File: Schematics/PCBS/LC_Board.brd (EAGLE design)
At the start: 160 x 100 mm, 24 parts, among them IC1 ATMEGA328P-AU, Q10 220mA/50V/3.5Ω, U1 LT1763CS8-3.3#TRPBF

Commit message: routing for PCB 1  ok outcome
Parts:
- RESET_PULLUP: device audio amplifier example:R0402 -> audio amplifier example:R0603
- moved RESET_PULLUP 26.9 mm to (44.5, 12.7)
- moved JP3 16.5 mm to (12.7, 39.4), turned to 0 degrees
- moved LED3BLUE 14.2 mm to (110.5, 12.7), turned to 180 degrees
- moved E1 13.5 mm to (43.2, 40.6), turned to 90 degrees
- moved LED1BLUE 13.3 mm to (110.5, 25.4), turned to 180 degrees
- moved LED3RED 13.3 mm to (110.5, 20.3)
- moved LED1RED 12.8 mm to (110.5, 33.0)
- moved LED2BLUE 12.8 mm to (110.5, 38.1), turned to 180 degrees
- moved LED2RED 12.8 mm to (110.5, 45.7)
- moved C1 11.4 mm to (19.2, 28.2), turned to 90 degrees
- moved LED3GREEN 10.2 mm to (106.7, 16.5), turned to 90 degrees
- moved E2 9.92 mm to (45.7, 40.6), turned to 90 degrees
- moved LED1GREEN 9.25 mm to (106.7, 29.2), turned to 90 degrees
- moved D3 8.98 mm to (110.5, 16.5)
- moved LED2GREEN 8.89 mm to (106.7, 41.9), turned to 90 degrees
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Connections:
- net N$1 renamed RED1
- net N$15 renamed RESET_LINE
- net N$2 renamed GREEN1
- net N$3 renamed BLUE1
- net N$4 renamed RED2
- net N$5 renamed GREEN2
- net N$6 renamed BLUE2
- net N$7 renamed RED3
- net N$8 renamed GREEN3
- net N$9 renamed BLUE3
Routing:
- net GND: track 0.00 -> 248.4 mm, vias 0 -> 1
- net 3.3V_RAIL: track 0.00 -> 204.9 mm
- net D5: track 0.00 -> 77.5 mm, vias 0 -> 2
- net D10: track 0.00 -> 75.2 mm, vias 0 -> 2
- net D8: track 0.00 -> 74.1 mm, vias 0 -> 2
- net D7: track 0.00 -> 72.6 mm, vias 0 -> 2
- net D9: track 0.00 -> 71.4 mm, vias 0 -> 2
- net D13: track 0.00 -> 68.8 mm
- net D6: track 0.00 -> 67.1 mm, vias 0 -> 2
- net D11: track 0.00 -> 65.9 mm, vias 0 -> 2
- net D12: track 0.00 -> 64.6 mm, vias 0 -> 2
- net RDI: track 0.00 -> 50.0 mm
- net TXO: track 0.00 -> 39.2 mm, vias 0 -> 1
- net RDI2: track 0.00 -> 34.9 mm
- net RESET_LINE: track 0.00 -> 34.2 mm
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
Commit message: LC_board PCB pos nearing finish for R1
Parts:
- moved JP2 73.8 mm to (86.4, 30.5), turned to 270 degrees
- moved C1 70.5 mm to (88.9, 17.8), turned to 180 degrees
- moved JP3 64.1 mm to (76.2, 30.5), turned to 90 degrees
- moved CONVERTEPULLUP 61.2 mm to (81.3, 26.7)
- moved Q10 61.0 mm to (81.3, 33.0)
- moved U1 54.6 mm to (83.8, 11.4)
- moved E1 50.9 mm to (94.0, 38.1)
- moved E2 50.9 mm to (96.5, 38.1)
- moved C2 50.8 mm to (96.4, 7.87)
- moved RESET_PULLUP 50.4 mm to (94.9, 11.7)
- moved IC1 49.5 mm to (94.0, 29.2)
- moved JP1 49.5 mm to (94.0, 2.54)
- moved LED1RED 14.0 mm to (110.5, 19.1)
- moved D1 14.0 mm to (110.5, 15.2), flipped to the bottom, turned to 180 degrees
- moved LED1GREEN 14.0 mm to (106.7, 15.2)
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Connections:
- net RXI2 renamed S$1
- net 3.3V_RAIL: no longer JP1.4
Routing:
- net GND: track 248.4 -> 136.4 mm, vias 1 -> 2
- net 3.3V_RAIL: track 204.9 -> 96.3 mm, vias 0 -> 3
- net D10: track 75.2 -> 0.00 mm, vias 2 -> 0
- net D13: track 68.8 -> 0.00 mm
- net D8: track 74.1 -> 7.75 mm, vias 2 -> 0
- net D11: track 65.9 -> 0.00 mm, vias 2 -> 0
- net D9: track 71.4 -> 6.27 mm, vias 2 -> 0
- net D12: track 64.6 -> 0.00 mm, vias 2 -> 0
- net D5: track 77.5 -> 26.7 mm
- net D6: track 67.1 -> 24.5 mm
- net D7: track 72.6 -> 30.7 mm
- net RDI: track 50.0 -> 33.6 mm
- net RDI2: track 34.9 -> 23.9 mm
- net RDI_3.3V: track 3.84 -> 12.3 mm
- net RESET_LINE: track 34.2 -> 36.3 mm, vias 0 -> 2
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
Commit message: back up be for remixing LED pos
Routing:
- net D8: track 7.75 -> 31.9 mm, vias 0 -> 1
- net D10: track 0.00 -> 23.0 mm, vias 0 -> 1
- net D11: track 0.00 -> 14.7 mm, vias 0 -> 1
- net D13: track 0.00 -> 13.5 mm, vias 0 -> 1
- net D9: track 6.27 -> 19.5 mm, vias 0 -> 1
- net D12: track 0.00 -> 12.6 mm, vias 0 -> 1
- net 3.3V_RAIL: track 96.3 -> 103.6 mm
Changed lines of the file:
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@@
 <wire x1="97.3853125" y1="27.4814" x2="96.8567125" y2="28.01" width="0.1524" layer="1"/>
 <contactref element="IC1" pad="6"/>
-<wire x1="96.8567125" y1="28.01" x2="93.98" y2="28.01" width="0.1524" layer="1"/>
-<wire x1="93.98" y1="28.01" x2="89.73" y2="28.01" width="0.1524" layer="1"/>
+<wire x1="96.8567125" y1="28.01" x2="95.25" y2="28.01" width="0.1524" layer="1"/>
+<wire x1="95.25" y1="28.01" x2="92.71" y2="28.01" width="0.1524" layer="1"/>
+<wire x1="92.71" y1="28.01" x2="89.73" y2="28.01" width="0.1524" layer="1"/>
 <wire x1="89.73" y1="28.01" x2="89.4586" y2="28.2814" width="0.1524" layer="1"/>
 <contactref element="C1" pad="+"/>
 <wire x1="90.17" y1="17.399" x2="89.789" y2="17.78" width="0.1524" layer="1"/>
 <contactref element="D3" pad="4"/>
-<wire x1="113.03" y1="27.94" x2="113.03" y2="21.59" width="0.1524" layer="16"/>
-<wire x1="113.03" y1="21.59" x2="113.03" y2="16.51" width="0.1524" layer="16"/>
-<wire x1="112.53" y1="28.44" x2="113.03" y2="27.94" width="0.1524" layer="16"/>
-<wire x1="112.53" y1="28.44" x2="111.19" y2="28.44" width="0.1524" layer="16"/>
-<wire x1="113.03" y1="27.94" x2="113.03" y2="40.64" width="0.1524" layer="16"/>
-<wire x1="113.03" y1="40.64" x2="112.53" y2="41.14" width="0.1524" layer="16"/>
-<wire x1="112.53" y1="41.14" x2="111.19" y2="41.14" width="0.1524" layer="16"/>
+<wire x1="114.3" y1="27.94" x2="114.3" y2="22.86" width="0.1524" layer="16"/>
+<wire x1="114.3" y1="20.32" x2="114.3" y2="16.51" width="0.1524" layer="16"/>
+<wire x1="113.8" y1="28.44" x2="114.3" y2="27.94" width="0.1524" layer="16"/>
+<wire x1="113.8" y1="28.44" x2="111.19" y2="28.44" width="0.1524" layer="16"/>
+<wire x1="114.3" y1="27.94" x2="114.3" y2="40.64" width="0.1524" layer="16"/>
+<wire x1="114.3" y1="40.64" x2="113.8" y2="41.14" width="0.1524" layer="16"/>
+<wire x1="113.8" y1="41.14" x2="111.19" y2="41.14" width="0.1524" layer="16"/>
 <contactref element="D1" pad="4"/>
 <wire x1="98.23" y1="27.21" x2="101.06" y2="27.21" width="0.1524" layer="1"/>
@@
 <via x="106.68" y="21.59" extent="1-16" drill="0.35" shape="octagon"/>
 <wire x1="106.68" y1="21.59" x2="113.03" y2="21.59" width="0.1524" layer="16"/>
-<wire x1="113.03" y1="16.51" x2="112.26" y2="15.74" width="0.1524" layer="16"/>
-<wire x1="112.26" y1="15.74" x2="111.19" y2="15.74" width="0.1524" layer="16"/>
+<wire x1="114.3" y1="16.51" x2="113.53" y2="15.74" width="0.1524" layer="16"/>
+<wire x1="113.53" y1="15.74" x2="111.19" y2="15.74" width="0.1524" layer="16"/>
 <wire x1="80.43" y1="26.67" x2="80.33" y2="26.77" width="0.1524" layer="1"/>
 <wire x1="80.33" y1="26.77" x2="80.33" y2="32.02" width="0.1524" layer="1"/>
@@
 <wire x1="93.98" y1="15.24" x2="93.98" y2="26.67" width="0.1524" layer="16"/>
 <via x="93.98" y="26.67" extent="1-16" drill="0.35" shape="octagon"/>
-<wire x1="93.98" y1="26.67" x2="93.98" y2="28.01" width="0.1524" layer="1"/>
 <contactref element="U1" pad="1"/>
 <wire x1="85.725" y1="13.8938" x2="89.6112" y2="17.78" width="0.1524" layer="1"/>
 <wire x1="89.6112" y1="17.78" x2="89.789" y2="17.78" width="0.1524" layer="1"/>
+<wire x1="113.03" y1="21.59" x2="114.3" y2="22.86" width="0.1524" layer="16"/>
+<wire x1="113.03" y1="21.59" x2="114.3" y2="20.32" width="0.1524" layer="16"/>
+<wire x1="92.71" y1="28.01" x2="93.98" y2="26.74" width="0.1524" layer="1"/>
+<wire x1="93.98" y1="26.74" x2="93.98" y2="26.67" width="0.1524" layer="1"/>
+<wire x1="95.25" y1="28.01" x2="95.25" y2="27.94" width="0.1524" layer="1"/>
+<wire x1="95.25" y1="27.94" x2="93.98" y2="26.67" width="0.1524" layer="1"/>
 <wire x1="97.79" y1="27.4814" x2="98.23" y2="27.21" width="0" layer="19" extent="1-1"/>
 <wire x1="80.43" y1="26.67" x2="89.73" y2="28.01" width="0" layer="19" extent="1-1"/>
@@
 <wire x1="99.06" y1="38.1" x2="96.52" y2="38.1" width="0.1524" layer="1"/>
 <wire x1="100.33" y1="29.61" x2="100.33" y2="36.83" width="0.1524" layer="1"/>
-<wire x1="110.49" y1="35.73" x2="110.49" y2="35.56" width="0" layer="19" extent="1-1"/>
+<wire x1="110.49" y1="45.55" x2="110.49" y2="35.56" width="0" layer="19" extent="1-1"/>
 <wire x1="97.79" y1="29.3386" x2="98.23" y2="29.61" width="0" layer="19" extent="1-1"/>
 <wire x1="83.185" y1="8.9662" x2="83.185" y2="8.255" width="0" layer="19" extent="1-1"/>
@@
 <contactref element="IC1" pad="13"/>
 <contactref element="LED2GREEN" pad="1"/>
-<wire x1="96.52" y1="20.32" x2="107.78" y2="39.69" width="0" layer="19" extent="1-1"/>
 <wire x1="94.38" y1="24.96" x2="94.38" y2="21.19" width="0.1524" layer="1"/>
 <wire x1="94.38" y1="21.19" x2="95.25" y2="20.32" width="0.1524" layer="1"/>
 <wire x1="95.25" y1="20.32" x2="96.52" y2="20.32" width="0.1524" layer="1"/>
+<wire x1="107.78" y1="39.69" x2="107.78" y2="39.2" width="0.1524" layer="1"/>
+<wire x1="107.78" y1="39.2" x2="106.68" y2="38.1" width="0.1524" layer="1"/>
+<via x="106.68" y="38.1" extent="1-16" drill="0.35" shape="octagon"/>
+<wire x1="106.68" y1="38.1" x2="105.41" y2="39.37" width="0.1524" layer="16"/>
+<wire x1="105.41" y1="39.37" x2="104.14" y2="39.37" width="0.1524" layer="16"/>
+<wire x1="104.14" y1="39.37" x2="102.87" y2="38.1" width="0.1524" layer="16"/>
+<wire x1="102.87" y1="38.1" x2="102.87" y2="31.75" width="0.1524" layer="16"/>
+<wire x1="94.38" y1="24.96" x2="102.87" y2="31.75" width="0" layer="19" extent="1-16"/>
 </signal>
 <signal name="D10">
 <contactref element="IC1" pad="14"/>
 <contactref element="LED2BLUE" pad="1"/>
-<wire x1="95.18" y1="24.96" x2="111.44" y2="37.93" width="0" layer="19" extent="1-1"/>
+<wire x1="95.18" y1="24.96" x2="95.18" y2="22.93" width="0.1524" layer="1"/>
+<wire x1="95.18" y1="22.93" x2="96.52" y2="21.59" width="0.1524" layer="1"/>
+<wire x1="96.52" y1="21.59" x2="100.33" y2="21.59" width="0.1524" layer="1"/>
+<wire x1="111.44" y1="37.93" x2="111.93" y2="37.93" width="0.1524" layer="1"/>
+<wire x1="111.93" y1="37.93" x2="113.03" y2="36.83" width="0.1524" layer="1"/>
+<via x="113.03" y="36.83" extent="1-16" drill="0.35" shape="octagon"/>
+<wire x1="113.03" y1="36.83" x2="105.41" y2="36.83" width="0.1524" layer="16"/>
+<wire x1="105.41" y1="36.83" x2="104.14" y2="35.56" width="0.1524" layer="16"/>
+<wire x1="104.14" y1="35.56" x2="104.14" y2="31.75" width="0.1524" layer="16"/>
+<wire x1="100.33" y1="21.59" x2="104.14" y2="31.75" width="0" layer="19" extent="1-16"/>
 </signal>
 <signal name="D11">
 <contactref element="IC1" pad="15"/>
 <contactref element="LED3RED" pad="1"/>
-<wire x1="95.98" y1="24.96" x2="109.54" y2="30.65" width="0" layer="19" extent="1-1"/>
+<wire x1="95.98" y1="24.96" x2="95.98" y2="23.4" width="0.1524" layer="1"/>
+<wire x1="95.98" y1="23.4" x2="96.52" y2="22.86" width="0.1524" layer="1"/>
+<wire x1="99.06" y1="22.86" x2="100.33" y2="24.13" width="0.1524" layer="1"/>
+<wire x1="96.52" y1="22.86" x2="99.06" y2="22.86" width="0.1524" layer="1"/>
+<wire x1="109.54" y1="30.65" x2="109.37" y2="30.48" width="0.1524" layer="1"/>
+<wire x1="109.37" y1="30.48" x2="107.95" y2="30.48" width="0.1524" layer="1"/>
+<via x="107.95" y="30.48" extent="1-16" drill="0.35" shape="octagon"/>
+<wire x1="107.95" y1="30.48" x2="101.6" y2="30.48" width="0.1524" layer="16"/>
+<wire x1="100.33" y1="24.13" x2="101.6" y2="30.48" width="0" layer="19" extent="1-16"/>
 </signal>
 <signal name="D12">
 <contactref element="IC1" pad="16"/>
 <contactref element="LED3GREEN" pad="1"/>
-<wire x1="96.78" y1="24.96" x2="107.78" y2="26.99" width="0" layer="19" extent="1-1"/>
+<wire x1="96.78" y1="24.96" x2="97.61" y2="24.13" width="0.1524" layer="1"/>
+<wire x1="97.61" y1="24.13" x2="99.06" y2="24.13" width="0.1524" layer="1"/>
+<wire x1="99.06" y1="24.13" x2="100.33" y2="25.4" width="0.1524" layer="1"/>
+<wire x1="107.78" y1="26.99" x2="107.78" y2="26.5" width="0.1524" layer="1"/>
+<wire x1="107.78" y1="26.5" x2="106.68" y2="25.4" width="0.1524" layer="1"/>
+<via x="106.68" y="25.4" extent="1-16" drill="0.35" shape="octagon"/>
+<wire x1="106.68" y1="25.4" x2="104.14" y2="27.94" width="0.1524" layer="16"/>
+<wire x1="104.14" y1="27.94" x2="101.6" y2="27.94" width="0.1524" layer="16"/>
+<wire x1="100.33" y1="25.4" x2="101.6" y2="27.94" width="0" layer="19" extent="1-16"/>
 </signal>
 <signal name="D13">
 <contactref element="IC1" pad="17"/>
 <contactref element="LED3BLUE" pad="1"/>
-<wire x1="98.23" y1="26.41" x2="111.44" y2="25.23" width="0" layer="19" extent="1-1"/>
+<wire x1="111.44" y1="25.23" x2="111.93" y2="25.23" width="0.1524" layer="1"/>
+<wire x1="111.93" y1="25.23" x2="113.03" y2="24.13" width="0.1524" layer="1"/>
+<via x="113.03" y="24.13" extent="1-16" drill="0.35" shape="octagon"/>
+<wire x1="113.03" y1="24.13" x2="101.6" y2="24.13" width="0.1524" layer="16"/>
+<wire x1="98.23" y1="26.41" x2="101.6" y2="24.13" width="0" layer="19" extent="1-16"/>
 </signal>
 <signal name="D8">
 <contactref element="IC1" pad="12"/>
 <contactref element="LED2RED" pad="1"/>
-<wire x1="96.519996875" y1="19.3548" x2="109.54" y2="43.35" width="0" layer="19" extent="1-1"/>
 <wire x1="93.58" y1="24.96" x2="93.58" y2="20.72" width="0.1524" layer="1"/>
 <wire x1="93.58" y1="20.72" x2="94.9452" y2="19.3548" width="0.1524" layer="1"/>
-<wire x1="94.9452" y1="19.3548" x2="96.519996875" y2="19.3548" width="0.1524" layer="1"/>
+<wire x1="100.6348" y1="19.3548" x2="101.6" y2="20.32" width="0.1524" layer="1"/>
+<wire x1="94.9452" y1="19.3548" x2="100.6348" y2="19.3548" width="0.1524" layer="1"/>
+<wire x1="109.54" y1="43.35" x2="109.37" y2="43.18" width="0.1524" layer="1"/>
+<wire x1="109.37" y1="43.18" x2="107.95" y2="43.18" width="0.1524" layer="1"/>
+<via x="107.95" y="43.18" extent="1-16" drill="0.35" shape="octagon"/>
+<wire x1="107.95" y1="43.18" x2="102.87" y2="43.18" width="0.1524" layer="16"/>
+<wire x1="102.87" y1="43.18" x2="101.6" y2="41.91" width="0.1524" layer="16"/>
+<wire x1="101.6" y1="41.91" x2="101.6" y2="31.75" width="0.1524" layer="16"/>
+<wire x1="101.6" y1="31.75" x2="93.58" y2="24.96" width="0" layer="19" extent="1-16"/>
 </signal>
 <signal name="RESET_LINE">

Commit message: Syncing schematic with board fixed
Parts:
- removed JP2: switching from 5v RDI to 3.3v RDI input, pinhead:1X03
- added SWITCHINGFROM5VRDITO3.3VRDIINPUT: Switch4RXI INPUT, pinhead:1X03
- moved CONVERTEPULLUP 5.68 mm to (86.4, 29.2), turned to 90 degrees
- moved Q10 5.08 mm to (81.3, 27.9), turned to 180 degrees
- moved JP3 3.81 mm to (76.2, 26.7)
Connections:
- net RDI2 renamed RXI2
- net S$1 renamed PULLED_UP3.3VRX
- removed net RDI: JP1.6, JP2.2
- removed net RDI_3.3V: JP2.3, JP3.1
- new net RXI: JP1.6, SWITCHINGFROM5VRDITO3.3VRDIINPUT.2
- new net RXI_3.3V: JP3.1, SWITCHINGFROM5VRDITO3.3VRDIINPUT.3
- net 3.3V_RAIL: now also JP1.4
- net D10: now also LED3BLUE.1; no longer LED2BLUE.1
- net D11: now also LED2GREEN.1; no longer LED3RED.1
- net D12: now also LED2RED.1; no longer LED3GREEN.1
- net D13: now also LED2BLUE.1; no longer LED3BLUE.1
- net D8: now also LED3RED.1; no longer LED2RED.1
- net D9: now also LED3GREEN.1; no longer LED2GREEN.1
- net RXD_IN: now also SWITCHINGFROM5VRDITO3.3VRDIINPUT.1; no longer JP2.1
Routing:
- net RDI: track 33.6 -> 0.00 mm
- net RXI: track 0.00 -> 31.1 mm
- net D12: track 12.6 -> 30.7 mm, vias 1 -> 2
- net D13: track 13.5 -> 29.0 mm, vias 1 -> 2
- net D11: track 14.7 -> 28.3 mm, vias 1 -> 2
- net 3.3V_RAIL: track 103.6 -> 116.9 mm
- net RDI_3.3V: track 12.3 -> 0.00 mm
- net PULLED_UP3.3VRX: track 18.1 -> 7.50 mm, vias 2 -> 0
- net RXI2: track 23.9 -> 30.7 mm
- net RXI_3.3V: track 0.00 -> 4.34 mm
- net GND: track 136.4 -> 139.4 mm
- net VIN: track 13.2 -> 15.7 mm
- net D8: track 31.9 -> 29.5 mm, vias 1 -> 2
- net RXD_IN: track 4.27 -> 5.61 mm
- net D9: track 19.5 -> 20.6 mm, vias 1 -> 2
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
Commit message: weekend backup
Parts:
- moved JP3 9.92 mm to (82.5, 34.3), turned to 0 degrees
- moved U1 3.81 mm to (87.6, 11.4)
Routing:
- net RXI2: track 30.7 -> 17.8 mm
- net RXI_3.3V: track 4.34 -> 12.5 mm
- net GND: track 139.4 -> 131.9 mm
- net PULLED_UP3.3VRX: track 7.50 -> 12.8 mm
- net VIN: track 15.7 -> 13.2 mm
- net 3.3V_RAIL: track 116.9 -> 115.6 mm
- net RXD_IN: track 5.61 -> 6.95 mm

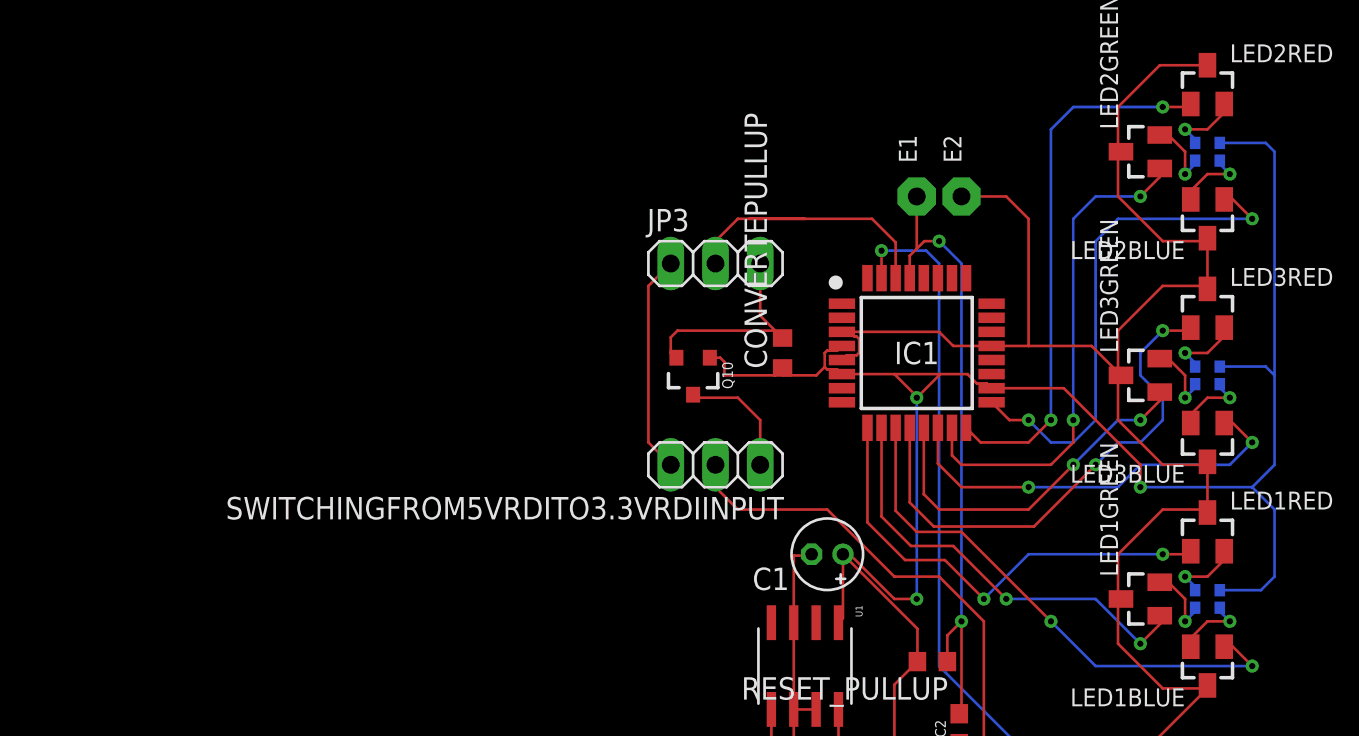
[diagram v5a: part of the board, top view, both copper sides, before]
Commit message: R1 Finish (yet to test)
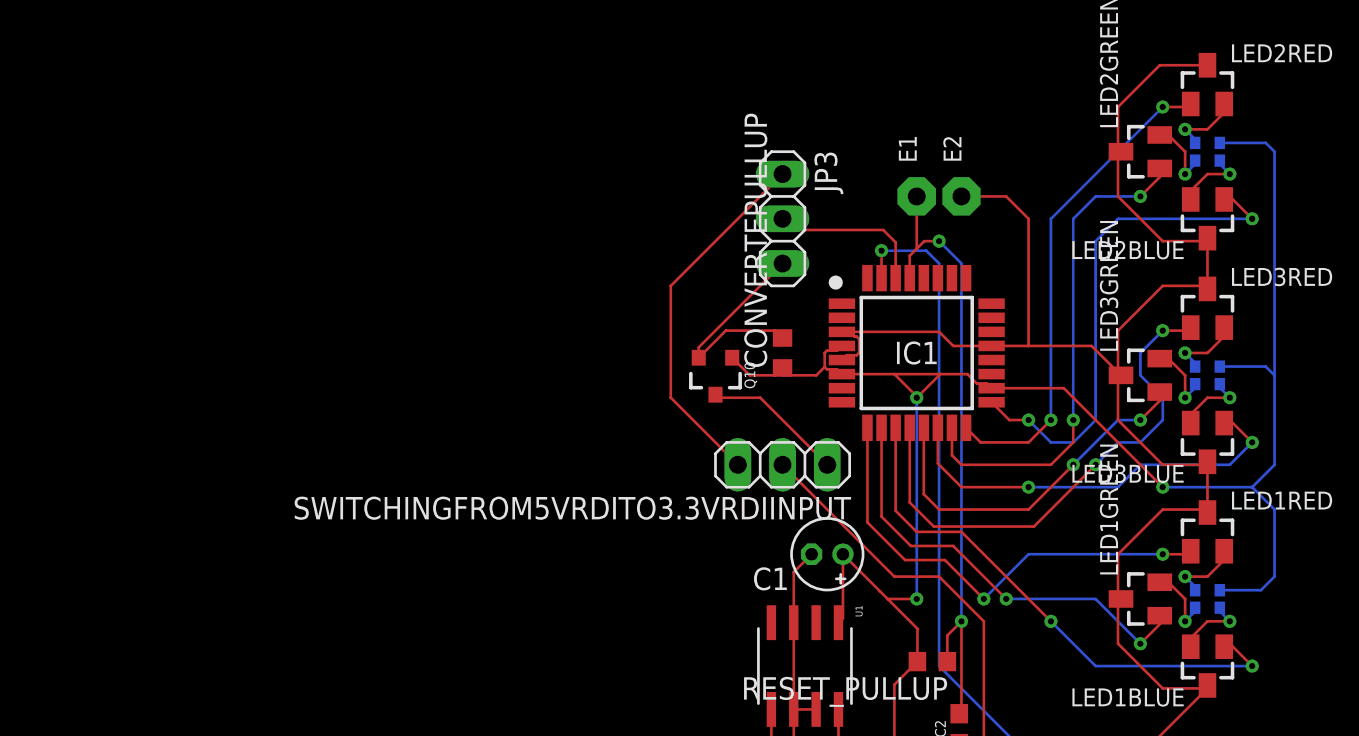
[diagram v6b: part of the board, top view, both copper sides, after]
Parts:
- moved JP3 4.58 mm to (86.4, 36.8), turned to 270 degrees
- moved SWITCHINGFROM5VRDITO3.3VRDIINPUT 3.81 mm to (86.4, 22.9)
- moved Q10 1.27 mm to (82.5, 27.9)
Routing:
- net RXI2: track 17.8 -> 9.01 mm
- net RXI_3.3V: track 12.5 -> 20.7 mm
- net 3.3V_RAIL: track 115.6 -> 109.5 mm
- net RXI: track 31.1 -> 26.5 mm
- net D12: track 30.7 -> 27.8 mm
- net RXD_IN: track 6.95 -> 8.00 mm
- net GND: track 131.9 -> 131.4 mm
